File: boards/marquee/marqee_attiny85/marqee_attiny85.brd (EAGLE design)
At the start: 37.9 x 24 mm, 11 parts, among them U1 ATTINY85-20PU

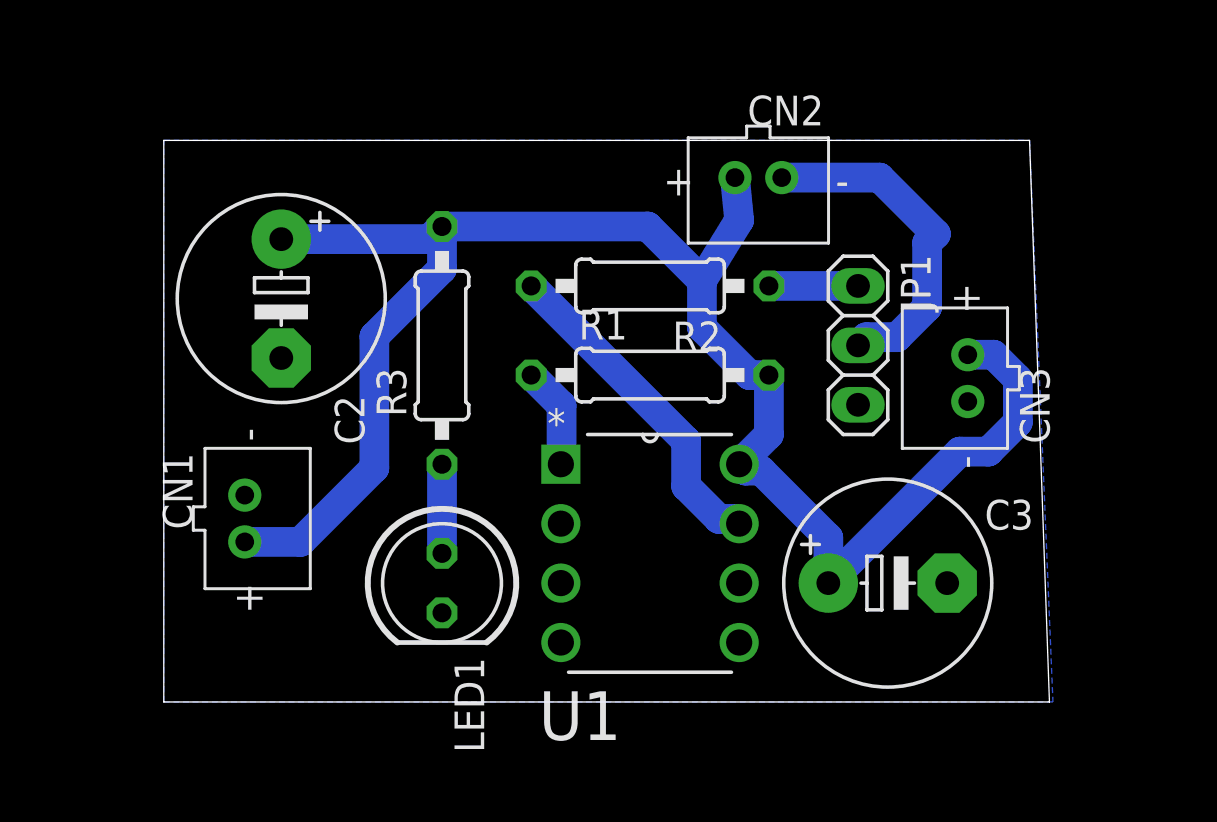
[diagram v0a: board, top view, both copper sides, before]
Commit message: class 3 materials; adds Arrow-NeoPixel PCB
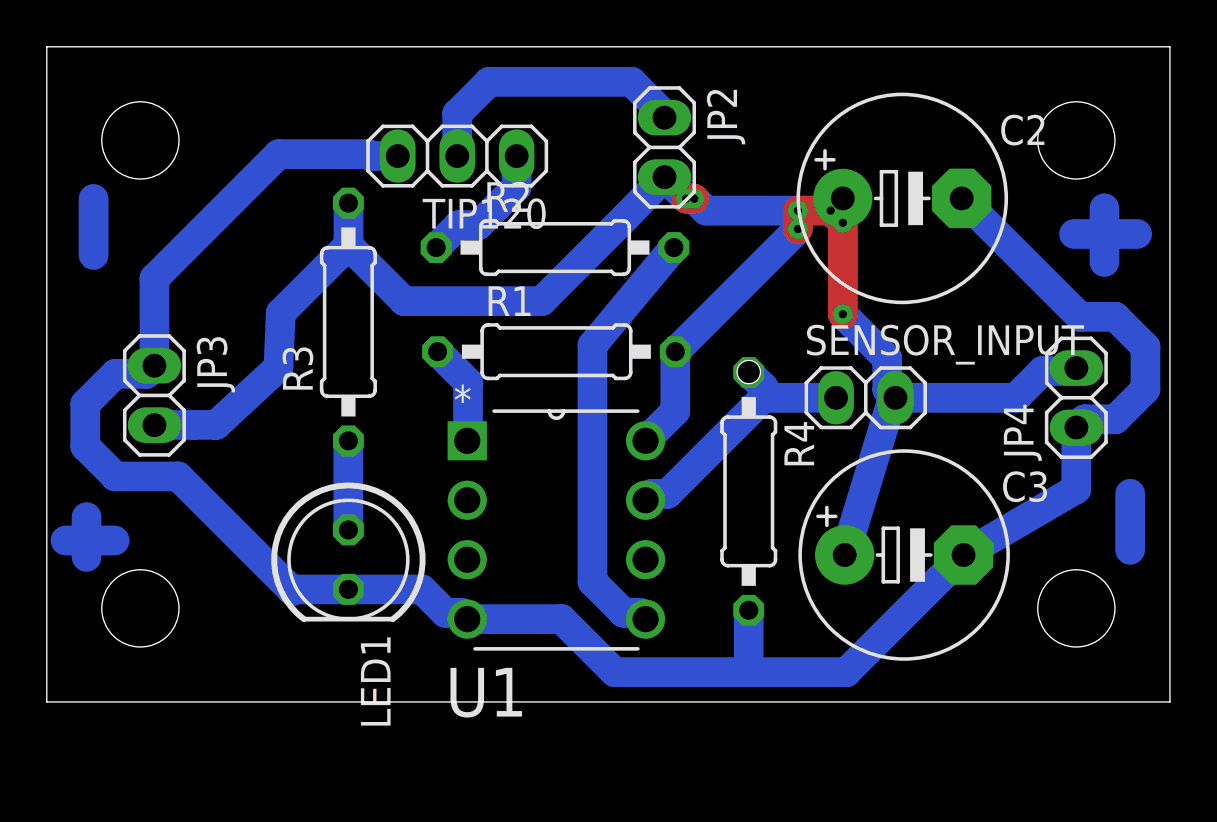
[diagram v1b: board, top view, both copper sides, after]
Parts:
- removed CN1, CN2, CN3: (no value), adafruit-2014:JST-PH-2-THM
- removed JP1: (no value), pinhead:1X03
- added JP2, JP3, JP4, SENSOR_INPUT: (no value), pinhead:1X02
- added R4: 1k, resistor:0207/10
- added TIP120: (no value), pinhead:1X03
- C2, C3: value (none) -> 47uF
- R1: value (none) -> 10k
- R2: value (none) -> 1k
- R3: value (none) -> 220
- moved C2 26.9 mm to (36.6, 21.5), turned to 0 degrees
- moved R2 4.38 mm to (21.7, 19.4), turned to 0 degrees
- moved LED1 4.12 mm to (12.9, 6.08)
- moved R1 4.12 mm to (21.8, 15.0)
- moved U1 4.12 mm to (25.6, 3.54)
- moved R3 4.12 mm to (12.9, 16.2)
- moved C3 1.39 mm to (36.6, 6.28)
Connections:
- removed net N$6: CN2.2, JP1.2
- new net ANALOG_SENSOR_IN: R4.1, SENSOR_INPUT.1, U1.7
- new net THING: JP2.1, TIP120.2
- net GND: now also JP3.1, JP4.1, R4.2, TIP120.3; no longer CN1.2, CN3.2, JP1.3
- net N$2: now also TIP120.1; no longer JP1.1
- net N$4: now also U1.5; no longer U1.7
- net VCC: now also JP2.2, JP3.2, JP4.2, SENSOR_INPUT.2; no longer CN1.1, CN2.1, CN3.1
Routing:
- net GND: track 0.00 -> 92.2 mm
- net N$6: track 14.5 -> 0.00 mm
- net THING: track 0.00 -> 12.0 mm
- net ANALOG_SENSOR_IN: track 0.00 -> 11.3 mm
- net N$4: track 14.2 -> 18.5 mm
- net N$8: track 0.00 -> 2.70 mm
- net N$9: track 0.00 -> 2.40 mm
- net N$10: track 0.00 -> 2.40 mm
- net N$7: track 0.00 -> 2.30 mm
- net N$12: track 0.00 -> 2.10 mm
- net N$2: track 3.81 -> 5.83 mm
- net VCC: track 74.8 -> 76.6 mm, vias 0 -> 7
- net N$11: track 0.00 -> 1.70 mm
- removed copper zone on layer 16, net GND
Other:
- board size 37.9 x 24 mm -> 48 x 28 mm
- board text added: "All Traces must be on the BOTTOM layer (blue) and any "air-wires" will be on the TOP layer (red)"
- board text added: "Holes are Nx10mm apart (so like 10mm, 20mm, 30mm, etc...)"
- board text added: "Holes have a 3.3mm Drill hole"
